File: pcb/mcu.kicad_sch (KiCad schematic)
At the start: 25 parts, among them CN9 2x5, IC2 STM32f103C8T, X1 H130B-8.000-18-3030-EXT-TR

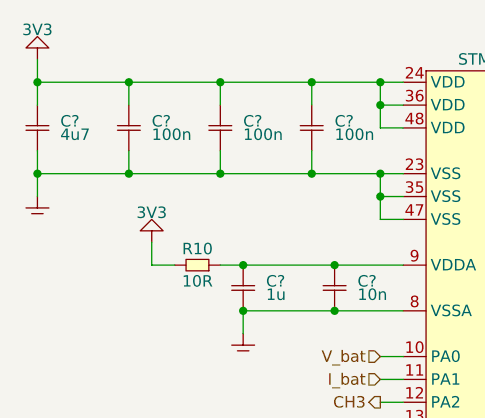
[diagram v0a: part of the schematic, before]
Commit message: updated component values
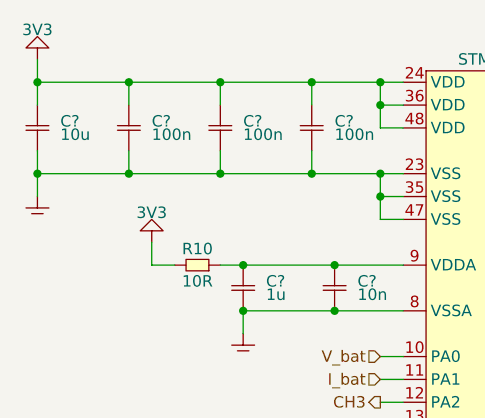
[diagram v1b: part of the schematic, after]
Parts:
- C?: value 4u7 -> 10u
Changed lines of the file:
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@@
       (effects (font (size 1.27 1.27)) (justify left bottom))
     )
-    (property "Value" "4u7" (at 96.52 71.12 0)
+    (property "Value" "10u" (at 96.52 71.12 0)
       (effects (font (size 1.27 1.27)) (justify left top))
     )

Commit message: worked on layout
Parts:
- added TP10, TP9: test_point, PCB:test_point, symbol PCB:test_point
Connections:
- net USB_N: no longer names the net of IC2.32 (PA11)
- net USB_N: now also TP9.1 (TP)
- net USB_P: no longer names the net of IC2.33 (PA12)
- net USB_P: now also TP10.1 (TP)
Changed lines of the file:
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@@
-    (stroke (width 0) (type default))
-  )
-  (wire (pts (xy 132.08 127) (xy 134.62 127))
     (stroke (width 0) (type default))
   )
@@
   )
   (wire (pts (xy 175.26 139.7) (xy 175.26 104.14))
-    (stroke (width 0) (type default))
-  )
-  (wire (pts (xy 132.08 124.46) (xy 134.62 124.46))
     (stroke (width 0) (type default))
   )
@@
     (effects (font (size 1.27 1.27)) (justify right))
   )
-  (hierarchical_label "USB_N" (shape bidirectional) (at 132.08 124.46 180) (fields_autoplaced)
-    (effects (font (size 1.27 1.27)) (justify right))
-  )
   (hierarchical_label "ADDR2" (shape input) (at 162.56 124.46 0) (fields_autoplaced)
     (effects (font (size 1.27 1.27)) (justify left))
   )
   (hierarchical_label "CH6" (shape output) (at 132.08 114.3 180) (fields_autoplaced)
-    (effects (font (size 1.27 1.27)) (justify right))
-  )
-  (hierarchical_label "USB_P" (shape bidirectional) (at 132.08 127 180) (fields_autoplaced)
     (effects (font (size 1.27 1.27)) (justify right))
   )
@@
     )
   )
+  (symbol (lib_id "PCB:test_point") (at 134.62 127 0) (mirror y) (unit 1)
+    (in_bom yes) (on_board yes) (dnp no)
+    (property "Reference" "TP10" (at 132.08 127 0)
+      (effects (font (size 1.27 1.27)) (justify left))
+    )
+    (property "Value" "test_point" (at 134.62 124.46 0)
+      (effects (font (size 1.27 1.27)) hide)
+    )
+    (property "Footprint" "PCB:test_point" (at 132.08 128.27 0)
+      (effects (font (size 1.27 1.27)) hide)
+    )
+    (property "Datasheet" "" (at 134.62 127 0)
+      (effects (font (size 1.27 1.27)) hide)
+    )
+    (pin "1")
+    (instances
+      (project "pcb"
+        (path "/6bb3bad6-1a89-4624-b34d-6ddda7dd16d2/19469851-aeaf-466c-9786-c0d0ae531cf4"
+          (reference "TP10") (unit 1)
+        )
+      )
+    )
+  )
   (symbol (lib_id "generic:C") (at 177.8 81.28 0) (mirror y) (unit 1)
     (in_bom yes) (on_board yes) (dnp no)
@@
         )
       )
+    )
+  )
+  (symbol (lib_id "PCB:test_point") (at 134.62 124.46 0) (mirror y) (unit 1)
+    (in_bom yes) (on_board yes) (dnp no)
+    (property "Reference" "TP9" (at 132.08 124.46 0)
+      (effects (font (size 1.27 1.27)) (justify left))
+    )
+    (property "Value" "test_point" (at 134.62 121.92 0)
+      (effects (font (size 1.27 1.27)) hide)
+    )
+    (property "Footprint" "PCB:test_point" (at 132.08 125.73 0)
+      (effects (font (size 1.27 1.27)) hide)
+    )
+    (property "Datasheet" "" (at 134.62 124.46 0)
+      (effects (font (size 1.27 1.27)) hide)
+    )
+    (pin "1")
+    (instances
+      (project "pcb"
+        (path "/6bb3bad6-1a89-4624-b34d-6ddda7dd16d2/19469851-aeaf-466c-9786-c0d0ae531cf4"
+          (reference "TP9") (unit 1)
+        )
+      )

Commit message: worked on pinout
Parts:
- removed C? (x2): 22p, SMT:0603, symbol generic:C
- removed TP1, TP10, TP2, TP3, TP4, TP7, TP8, TP9: test_point, PCB:test_point, symbol PCB:test_point
- removed X1: H130B-8.000-18-3030-EXT-TR, xtal:5x3.2, symbol generic:xtal_gnd
- renumbered TP13 to TP2, TP12 to TP3, TP14 to TP4
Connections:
- net IN_6: now reaches IC2.40 (PB4)
- net IN_1: now reaches IC2.14 (PA4)
- net IN_5: now reaches IC2.20 (PB2)
- net at TP6.1 (TP): now also IC2.28 (PB15); no longer IC2.26 (PB13)
- net at IC2.27 (PB14): now also TP5.1 (TP)
- net IN_2: now reaches IC2.31 (PA10)
- net IN_3: now reaches IC2.32 (PA11)
- net IN_4: now reaches IC2.33 (PA12)
- net IN_7: now reaches IC2.41 (PB5)
- net IN_7: no longer TP5.1 (TP)
- new net IN_8: IC2.26 (PB13)
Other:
- moved on the sheet: C?, R10

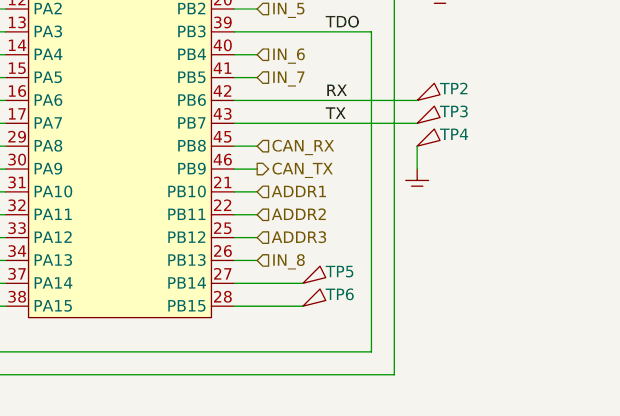
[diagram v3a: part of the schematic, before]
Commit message: added hierarchial sheets for buffering
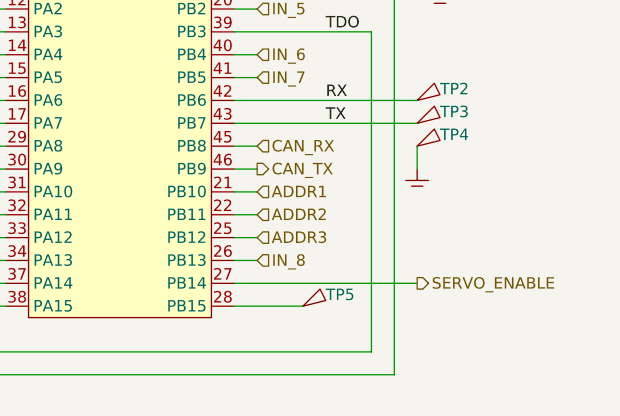
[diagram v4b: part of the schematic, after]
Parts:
- removed TP6: test_point, PCB:test_point, symbol PCB:test_point
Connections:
- net at TP5.1 (TP): now also IC2.28 (PB15); no longer IC2.27 (PB14)
- new net SERVO_ENABLE: IC2.27 (PB14)
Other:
- moved on the sheet: TP5
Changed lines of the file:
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@@
-    (stroke (width 0) (type default))
-  )
-  (wire (pts (xy 160.02 132.08) (xy 167.64 132.08))
     (stroke (width 0) (type default))
   )
@@
     (stroke (width 0) (type default))
   )
+  (wire (pts (xy 160.02 132.08) (xy 180.34 132.08))
+    (stroke (width 0) (type default))
+  )
   (wire (pts (xy 162.56 106.68) (xy 160.02 106.68))
     (stroke (width 0) (type default))
@@
   )
   (hierarchical_label "ADDR1" (shape input) (at 162.56 121.92 0) (fields_autoplaced)
+    (effects (font (size 1.27 1.27)) (justify left))
+  )
+  (hierarchical_label "SERVO_ENABLE" (shape output) (at 180.34 132.08 0) (fields_autoplaced)
     (effects (font (size 1.27 1.27)) (justify left))
   )
@@
     )
   )
-  (symbol (lib_id "PCB:test_point") (at 167.64 132.08 0) (unit 1)
+  (symbol (lib_id "PCB:test_point") (at 167.64 134.62 0) (unit 1)
     (in_bom yes) (on_board yes) (dnp no)
-    (property "Reference" "TP5" (at 170.18 130.81 0)
+    (property "Reference" "TP5" (at 170.18 133.35 0)
       (effects (font (size 1.27 1.27)) (justify left))
     )
-    (property "Value" "test_point" (at 167.64 129.54 0)
-      (effects (font (size 1.27 1.27)) hide)
-    )
-    (property "Footprint" "PCB:test_point" (at 170.18 133.35 0)
-      (effects (font (size 1.27 1.27)) hide)
-    )
-    (property "Datasheet" "" (at 167.64 132.08 0)
+    (property "Value" "test_point" (at 167.64 132.08 0)
+      (effects (font (size 1.27 1.27)) hide)
+    )
+    (property "Footprint" "PCB:test_point" (at 170.18 135.89 0)
+      (effects (font (size 1.27 1.27)) hide)
+    )
+    (property "Datasheet" "" (at 167.64 134.62 0)
       (effects (font (size 1.27 1.27)) hide)
     )
@@
         )
       )
-    )
-  )
-  (symbol (lib_id "PCB:test_point") (at 167.64 134.62 0) (unit 1)
-    (in_bom yes) (on_board yes) (dnp no)
-    (property "Reference" "TP6" (at 170.18 133.35 0)
-      (effects (font (size 1.27 1.27)) (justify left))
-    )
-    (property "Value" "test_point" (at 167.64 132.08 0)
-      (effects (font (size 1.27 1.27)) hide)
-    )
-    (property "Footprint" "PCB:test_point" (at 170.18 135.89 0)
-      (effects (font (size 1.27 1.27)) hide)
-    )
-    (property "Datasheet" "" (at 167.64 134.62 0)
-      (effects (font (size 1.27 1.27)) hide)
-    )
-    (pin "1")
-    (instances
-      (project "pcb"
-        (path "/6bb3bad6-1a89-4624-b34d-6ddda7dd16d2/19469851-aeaf-466c-9786-c0d0ae531cf4"
-          (reference "TP6") (unit 1)
-        )
-      )

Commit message: worked on layout
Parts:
- gave numbers to parts that had none: 7
- renumbered R10 to R16, R10 to R3
